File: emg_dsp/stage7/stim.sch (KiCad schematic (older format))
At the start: 7 parts

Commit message: woooo working on the next microstimulator.
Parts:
- removed U?: JUMP, 2x100mil, symbol JUMP
- added D2: D, SOD-323, symbol D
- added R5: 1k, 0402, symbol R
- added TP1: TP, TP, symbol TP
- gave numbers to parts that had none: 6
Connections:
- net Iout: now also R5.1; no longer U12.3 (FB)
- net at C19.1, D1.3 (c): now also U13.3 (d), D2.3 (c), TP1.1
- new net: D2.1 (a), R5.2, U12.3 (FB)
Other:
- note added: "30V Zener"
- note added: "eg BZT52C30S"
- moved on the sheet: C47, U41

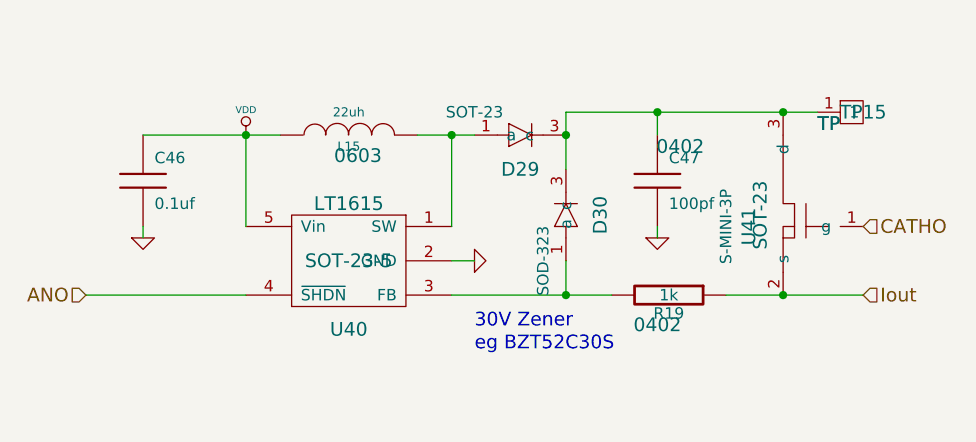
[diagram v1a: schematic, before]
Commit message: wireless stimulator!
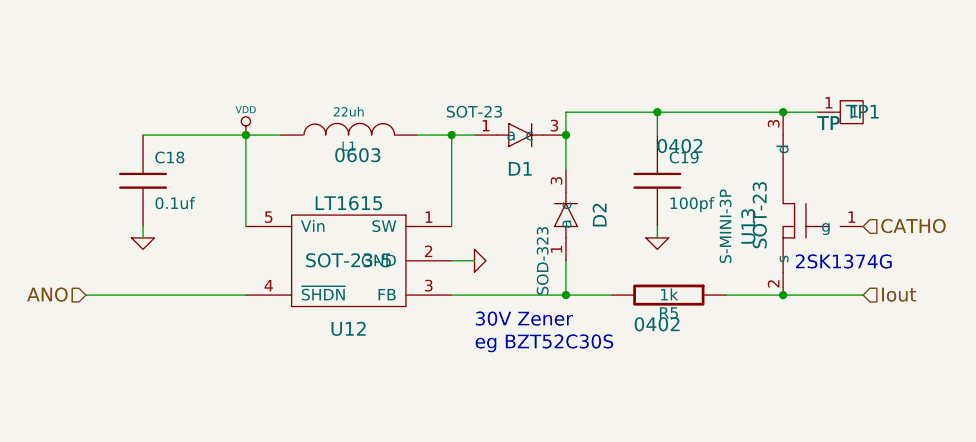
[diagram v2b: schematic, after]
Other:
- note added: "2SK1374G"
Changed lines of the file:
@@
-EESchema Schematic File Version 2  date Tue 14 Dec 2010 04:38:47 PM EST
+EESchema Schematic File Version 2  date Tue 14 Dec 2010 05:53:46 PM EST
 LIBS:power
 LIBS:device
@@
 EELAYER END
 $Descr A4 11700 8267
-Sheet 9 16
+Sheet 16 16
 Title ""
 Date "14 dec 2010"
@@
 Comment4 ""
 $EndDescr
+Text Notes 7300 3200 0    60   ~ 0
+2SK1374G
 Text Notes 5900 3550 0    60   ~ 0
 eg BZT52C30S
@@
 AR Path="/4CFFF121/4D07D318" Ref="R7"  Part="1"
 AR Path="/4CFFF11C/4D07D318" Ref="R6"  Part="1"
-F 0 "R19" V 6830 3300 50  0000 C CNN
+F 0 "R5" V 6830 3300 50  0000 C CNN
 F 1 "1k" V 6750 3300 50  0000 C CNN
 F 2 "0402" V 6880 3250 60  0000 C CNN
@@
 AR Path="/4CFFF121/4D07D2DB" Ref="D6"  Part="1"
 AR Path="/4CFFF11C/4D07D2DB" Ref="D4"  Part="1"
-F 0 "D30" H 6300 3100 60  0000 C CNN
+F 0 "D2" H 6300 3100 60  0000 C CNN
 F 1 "D" H 6300 2800 60  0001 C CNN
 F 2 "SOD-323" H 6500 2850 50  0000 C CNN
@@
 AR Path="/4CFFF121/4D07C82A" Ref="TP3"  Part="1"
 AR Path="/4CFFF11C/4D07C82A" Ref="TP2"  Part="1"
-F 0 "TP15" H 7600 2500 60  0000 C CNN
+F 0 "TP1" H 7600 2500 60  0000 C CNN
 F 1 "TP" H 7450 2450 60  0000 C CNN
 F 2 "TP" H 7450 2450 60  0000 C CNN
@@
 AR Path="/4CFFF124/4CFFEDFB" Ref="U19"  Part="1"
 AR Path="/4CFFF121/4CFFEDFB" Ref="U17"  Part="1"
-F 0 "U41" H 7000 3100 60  0000 C CNN
+F 0 "U13" H 7000 3100 60  0000 C CNN
 F 1 "SOT-23" H 7050 3150 60  0000 C CNN
 F 2 "S-MINI-3P" H 7000 3000 50  0000 C CNN
@@
 AR Path="/4CFFF124/4CFFEA48" Ref="C24"  Part="1"
 AR Path="/4CFFF121/4CFFEA48" Ref="C22"  Part="1"
-F 0 "C46" H 4500 2900 50  0000 L CNN
+F 0 "C18" H 4500 2900 50  0000 L CNN
 F 1 "0.1uf" H 4500 2700 50  0000 L CNN
 F 2 "0402" H 4550 2950 60  0001 C CNN
@@
 AR Path="/4CFFF124/4CFFEA24" Ref="C25"  Part="1"
 AR Path="/4CFFF121/4CFFEA24" Ref="C23"  Part="1"
-F 0 "C47" H 6750 2900 50  0000 L CNN
+F 0 "C19" H 6750 2900 50  0000 L CNN
 F 1 "100pf" H 6750 2700 50  0000 L CNN
 F 2 "0402" H 6800 2950 60  0000 C CNN
@@
 AR Path="/4CFFF124/4CFFE9AE" Ref="D7"  Part="1"
 AR Path="/4CFFF121/4CFFE9AE" Ref="D5"  Part="1"
-F 0 "D29" H 6100 2750 60  0000 C CNN
+F 0 "D1" H 6100 2750 60  0000 C CNN
 F 1 "BAT54" H 6100 2450 60  0001 C CNN
 F 2 "SOT-23" H 6300 2500 50  0000 C CNN
@@
 AR Path="/4CFFF124/4CFFE99A" Ref="L4"  Part="1"
 AR Path="/4CFFF121/4CFFE99A" Ref="L3"  Part="1"
-F 0 "L15" V 5300 2600 40  0000 C CNN
+F 0 "L1" V 5300 2600 40  0000 C CNN
 F 1 "22uh" V 5450 2600 40  0000 C CNN
 F 2 "0603" V 5260 2560 60  0000 C CNN
@@
 AR Path="/4CFFF124/4CFFE988" Ref="U18"  Part="1"
 AR Path="/4CFFF121/4CFFE988" Ref="U16"  Part="1"
-F 0 "U40" H 5350 2850 60  0000 C CNN
+F 0 "U12" H 5350 2850 60  0000 C CNN
 F 1 "LT1615" H 5350 3400 60  0000 C CNN
 F 2 "SOT-23-5" H 5350 3150 60  0000 C CNN

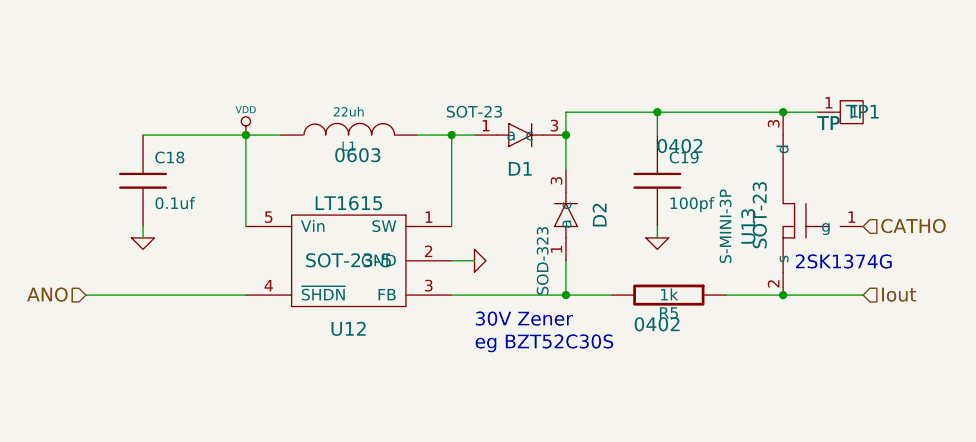
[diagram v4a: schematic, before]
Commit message: adding changes to new board -- still feel that the schematic needs to be checked over, though.
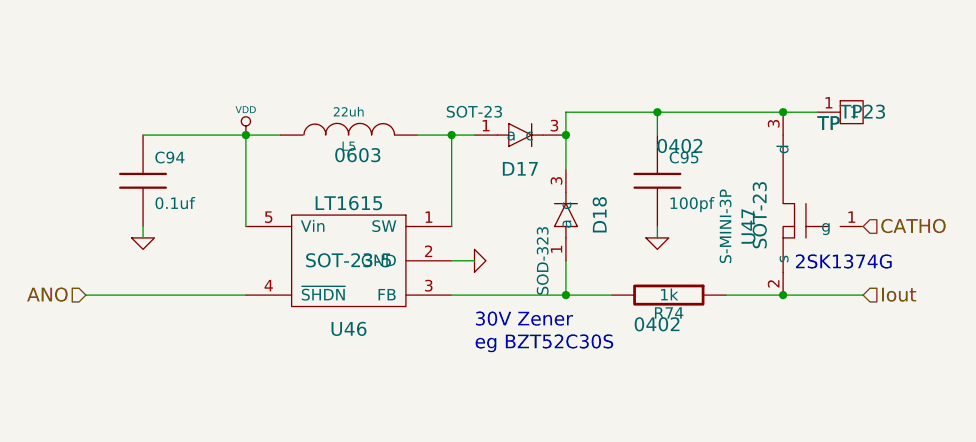
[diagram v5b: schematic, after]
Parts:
- removed C18: 0.1uf, 0402, symbol C
- removed C19: 100pf, 0402, symbol C
- removed D1: BAT54, SOT-23, symbol D
- removed D2: D, SOD-323, symbol D
- removed L1: 22uh, 0603, symbol INDUCTOR
- removed R5: 1k, 0402, symbol R
- removed TP1: TP, TP, symbol TP
- removed U13: SOT-23, S-MINI-3P, symbol 2SK3539
- added C94: 0.1uf, 0402, symbol C
- added C95: 100pf, 0402, symbol C
- added D17: BAT54, SOT-23, symbol D
- added D18: D, SOD-323, symbol D
- added L5: 22uh, 0603, symbol INDUCTOR
- added R74: 1k, 0402, symbol R
- added TP23: TP, TP, symbol TP
- added U47: SOT-23, S-MINI-3P, symbol 2SK3539
- renumbered U12 to U46
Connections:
- net CATHO: now also U47.1 (g)
- net GND: now also C94.2, C95.2
- net Iout: now also R74.1, U47.2 (s)
- net VDD: now also C94.1, L5.1
- net at U46.1 (SW): now also D17.1 (a), L5.2
- net at U46.3 (FB): now also D18.1 (a), R74.2
- new net: C95.1, D17.3 (c), D18.3 (c), TP23.1, U47.3 (d)

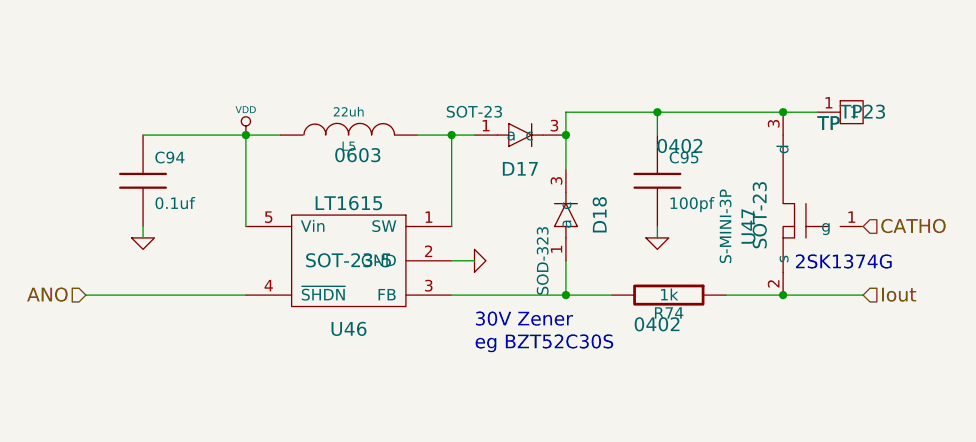
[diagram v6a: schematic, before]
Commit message: working on the stimulator - using battery isolation for now. the Burr-brown DC-DC converters tend to generate a bit of noise.
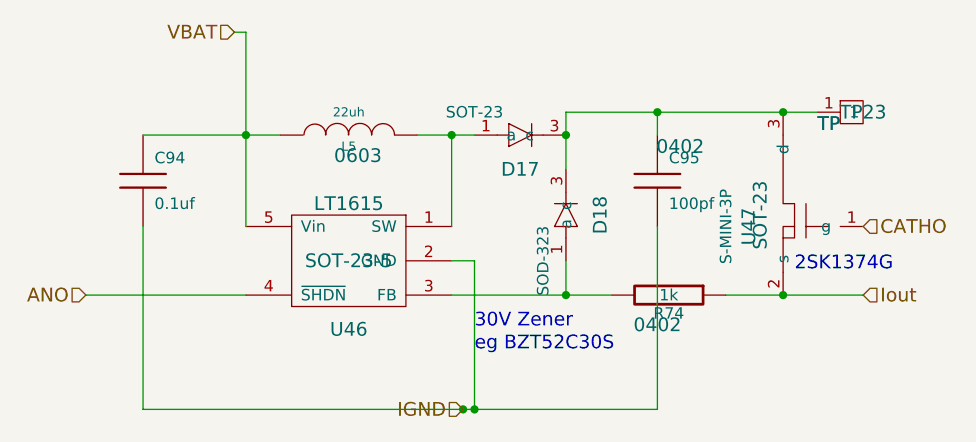
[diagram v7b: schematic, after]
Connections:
- net GND renamed IGND
- net VDD renamed VBAT
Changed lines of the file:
@@
-EESchema Schematic File Version 2  date Fri 21 Jan 2011 02:51:55 PM EST
+EESchema Schematic File Version 2  date Fri 21 Jan 2011 05:22:11 PM EST
 LIBS:power
 LIBS:device
@@
 EELAYER END
 $Descr A4 11700 8267
-Sheet 11 19
+Sheet 13 19
 Title ""
-Date "20 jan 2011"
+Date "21 jan 2011"
 Rev ""
 Comp ""
@@
 Comment4 ""
 $EndDescr
+Connection ~ 5850 3800
+Wire Wire Line
+	4450 3800 6700 3800
+Wire Wire Line
+	4450 3800 4450 3000
+Wire Wire Line
+	4900 3000 4900 2150
+Wire Wire Line
+	4900 2150 4850 2150
+Wire Wire Line
+	7600 3300 7000 3300
+Wire Wire Line
+	5800 3300 6500 3300
+Connection ~ 6300 2600
+Wire Wire Line
+	6300 2750 6300 2500
+Wire Wire Line
+	4900 3300 4200 3300
+Connection ~ 4900 2600
+Wire Wire Line
+	4450 2600 5050 2600
+Wire Wire Line
+	5800 3150 5900 3150
+Wire Wire Line
+	5650 2600 5900 2600
+Wire Wire Line
+	5800 3000 5800 2600
+Connection ~ 5800 2600
+Connection ~ 7250 3300
+Connection ~ 7250 2500
+Wire Wire Line
+	6300 2500 7400 2500
+Wire Wire Line
+	6300 3300 6300 3150
+Connection ~ 6300 3300
+Wire Wire Line
+	6700 2600 6700 2500
+Connection ~ 6700 2500
+Wire Wire Line
+	5900 3150 5900 3800
+Wire Wire Line
+	6700 3800 6700 3000
+Connection ~ 5900 3800
+Text HLabel 5850 3800 0    60   Input ~ 0
+IGND
+Text HLabel 4850 2150 0    60   Input ~ 0
+VBAT
 Text Notes 7300 3200 0    60   ~ 0
 2SK1374G
@@
 Text Notes 5900 3450 0    60   ~ 0
 30V Zener
-Wire Wire Line
-	7600 3300 7000 3300
-Wire Wire Line
-	5800 3300 6500 3300
-Wire Wire Line
-	6700 3000 6700 3050
-Connection ~ 6300 2600
-Wire Wire Line
-	6300 2750 6300 2500
-Wire Wire Line
-	4900 3300 4200 3300
-Connection ~ 4900 2600
-Wire Wire Line
-	4450 2600 5050 2600
-Wire Wire Line
-	5800 3150 5900 3150
-Wire Wire Line
-	5650 2600 5900 2600
-Wire Wire Line
-	5800 3000 5800 2600
-Connection ~ 5800 2600
-Wire Wire Line
-	4900 2600 4900 3000
-Wire Wire Line
-	4450 3000 4450 3050
-Connection ~ 7250 3300
-Connection ~ 7250 2500
-Wire Wire Line
-	6300 2500 7400 2500
-Wire Wire Line
-	6300 3300 6300 3150
-Connection ~ 6300 3300
-Wire Wire Line
-	6700 2600 6700 2500
-Connection ~ 6700 2500
 $Comp
 L R R74
@@
 AR Path="/4D2F608C/4CFFFADB/4D361954" Ref="R74"  Part="1"
 AR Path="/4D2F608C/4CFFE972/4D361954" Ref="R74"  Part="1"
+AR Path="/4D2F608C/4D07DB98/4D361954" Ref="R74"  Part="1"
+AR Path="/4D2F608C/4CFFF11C/4D361954" Ref="R74"  Part="1"
+AR Path="/4D2F608C/4CFFFADE/4D361954" Ref="R74"  Part="1"
 F 0 "R74" V 6830 3300 50  0000 C CNN
 F 1 "1k" V 6750 3300 50  0000 C CNN
@@
 AR Path="/4D2F608C/4CFFFADB/4D36194B" Ref="D18"  Part="1"
 AR Path="/4D2F608C/4CFFE972/4D36194B" Ref="D18"  Part="1"
+AR Path="/4D2F608C/4D07DB98/4D36194B" Ref="D18"  Part="1"
+AR Path="/4D2F608C/4CFFF11C/4D36194B" Ref="D18"  Part="1"
+AR Path="/4D2F608C/4CFFFADE/4D36194B" Ref="D18"  Part="1"
 F 0 "D18" H 6300 3100 60  0000 C CNN
 F 1 "D" H 6300 2800 60  0001 C CNN
@@
 AR Path="/4D2F608C/4CFFFADB/4D361938" Ref="TP23"  Part="1"
 AR Path="/4D2F608C/4CFFE972/4D361938" Ref="TP23"  Part="1"
+AR Path="/4D2F608C/4D07DB98/4D361938" Ref="TP23"  Part="1"
+AR Path="/4D2F608C/4CFFF11C/4D361938" Ref="TP23"  Part="1"
+AR Path="/4D2F608C/4CFFFADE/4D361938" Ref="TP23"  Part="1"
 F 0 "TP23" H 7600 2500 60  0000 C CNN
 F 1 "TP" H 7450 2450 60  0000 C CNN
@@
 $EndComp
 $Comp
-L VDD #PWR0218
-U 1 1 4D361928
-P 4900 2600
-AR Path="/4D2F608C/4CFFFADB/4D361928" Ref="#PWR0218"  Part="1"
-AR Path="/4D2F608C/4CFFE972/4D361928" Ref="#PWR0218"  Part="1"
-F 0 "#PWR0218" H 4900 2700 30  0001 C CNN
-F 1 "VDD" H 4900 2710 30  0000 C CNN
-	1    4900 2600
-	1    0    0    -1
-$EndComp
-$Comp
 L 2SK3539 U47
 U 1 1 4D361921
@@
 AR Path="/4D2F608C/4CFFFADB/4D361921" Ref="U47"  Part="1"
 AR Path="/4D2F608C/4CFFE972/4D361921" Ref="U47"  Part="1"
+AR Path="/4D2F608C/4D07DB98/4D361921" Ref="U47"  Part="1"
+AR Path="/4D2F608C/4CFFF11C/4D361921" Ref="U47"  Part="1"
+AR Path="/4D2F608C/4CFFFADE/4D361921" Ref="U47"  Part="1"
 F 0 "U47" H 7000 3100 60  0000 C CNN
 F 1 "SOT-23" H 7050 3150 60  0000 C CNN
@@
 $EndComp
 $Comp
-L GND #PWR0219
-U 1 1 4D361919
-P 4450 3050
-AR Path="/4D2F608C/4CFFFADB/4D361919" Ref="#PWR0219"  Part="1"
-AR Path="/4D2F608C/4CFFE972/4D361919" Ref="#PWR0219"  Part="1"
-F 0 "#PWR0219" H 4450 3050 30  0001 C CNN
-F 1 "GND" H 4450 2980 30  0001 C CNN
-	1    4450 3050
-	1    0    0    -1
-$EndComp
-$Comp
 L C C94
 U 1 1 4D36190A
@@
 AR Path="/4D2F608C/4CFFFADB/4D36190A" Ref="C94"  Part="1"
 AR Path="/4D2F608C/4CFFE972/4D36190A" Ref="C94"  Part="1"
+AR Path="/4D2F608C/4D07DB98/4D36190A" Ref="C94"  Part="1"
+AR Path="/4D2F608C/4CFFF11C/4D36190A" Ref="C94"  Part="1"
+AR Path="/4D2F608C/4CFFFADE/4D36190A" Ref="C94"  Part="1"
 F 0 "C94" H 4500 2900 50  0000 L CNN
 F 1 "0.1uf" H 4500 2700 50  0000 L CNN
@@
 $EndComp
 $Comp
-L GND #PWR0220
-U 1 1 4D3618FA
-P 6700 3050
-AR Path="/4D2F608C/4CFFFADB/4D3618FA" Ref="#PWR0220"  Part="1"
-AR Path="/4D2F608C/4CFFE972/4D3618FA" Ref="#PWR0220"  Part="1"
-F 0 "#PWR0220" H 6700 3050 30  0001 C CNN
-F 1 "GND" H 6700 2980 30  0001 C CNN
-	1    6700 3050
-	1    0    0    -1
-$EndComp
-$Comp
 L C C95
 U 1 1 4D3618E7
@@
 AR Path="/4D2F608C/4CFFFADB/4D3618E7" Ref="C95"  Part="1"
 AR Path="/4D2F608C/4CFFE972/4D3618E7" Ref="C95"  Part="1"
+AR Path="/4D2F608C/4D07DB98/4D3618E7" Ref="C95"  Part="1"
+AR Path="/4D2F608C/4CFFF11C/4D3618E7" Ref="C95"  Part="1"
+AR Path="/4D2F608C/4CFFFADE/4D3618E7" Ref="C95"  Part="1"
 F 0 "C95" H 6750 2900 50  0000 L CNN
 F 1 "100pf" H 6750 2700 50  0000 L CNN
@@
 ANO
 $Comp
-L GND #PWR0221
-U 1 1 4D3618D6
-P 5900 3150
-AR Path="/4D2F608C/4CFFFADB/4D3618D6" Ref="#PWR0221"  Part="1"
-AR Path="/4D2F608C/4CFFE972/4D3618D6" Ref="#PWR0221"  Part="1"
-F 0 "#PWR0221" H 5900 3150 30  0001 C CNN
-F 1 "GND" H 5900 3080 30  0001 C CNN
-	1    5900 3150
-	0    -1   -1   0
-$EndComp
-$Comp
 L D D17
 U 1 1 4D3618C7
@@
 AR Path="/4D2F608C/4CFFFADB/4D3618C7" Ref="D17"  Part="1"
 AR Path="/4D2F608C/4CFFE972/4D3618C7" Ref="D17"  Part="1"
+AR Path="/4D2F608C/4D07DB98/4D3618C7" Ref="D17"  Part="1"
+AR Path="/4D2F608C/4CFFF11C/4D3618C7" Ref="D17"  Part="1"
+AR Path="/4D2F608C/4CFFFADE/4D3618C7" Ref="D17"  Part="1"
 F 0 "D17" H 6100 2750 60  0000 C CNN
 F 1 "BAT54" H 6100 2450 60  0001 C CNN
@@
 AR Path="/4D2F608C/4CFFFADB/4D3618C2" Ref="L5"  Part="1"
 AR Path="/4D2F608C/4CFFE972/4D3618C2" Ref="L5"  Part="1"
+AR Path="/4D2F608C/4D07DB98/4D3618C2" Ref="L5"  Part="1"
+AR Path="/4D2F608C/4CFFF11C/4D3618C2" Ref="L5"  Part="1"
+AR Path="/4D2F608C/4CFFFADE/4D3618C2" Ref="L5"  Part="1"
 F 0 "L5" V 5300 2600 40  0000 C CNN
 F 1 "22uh" V 5450 2600 40  0000 C CNN
@@
 AR Path="/4D2F608C/4CFFFADB/4CFFE988" Ref="U46"  Part="1"
 AR Path="/4D2F608C/4CFFE972/4CFFE988" Ref="U46"  Part="1"
+AR Path="/4D2F608C/4D07DB98/4CFFE988" Ref="U46"  Part="1"
+AR Path="/4D2F608C/4CFFF11C/4CFFE988" Ref="U46"  Part="1"
+AR Path="/4D2F608C/4CFFFADE/4CFFE988" Ref="U46"  Part="1"
 F 0 "U46" H 5350 2850 60  0000 C CNN
 F 1 "LT1615" H 5350 3400 60  0000 C CNN

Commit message: starting placement of modules in board...
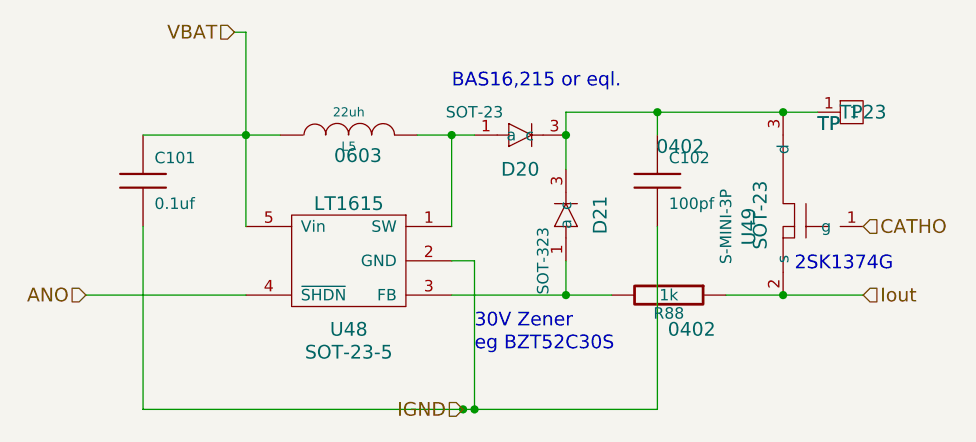
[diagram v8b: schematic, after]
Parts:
- D49: renamed from D18; footprint SOD-323 -> SOT-323
- renumbered C94 to C129, C95 to C130, D17 to D48, L5 to L19, R74 to R102, TP23 to TP37, U46 to U76, U47 to U77
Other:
- note added: "BAS16,215 or eql."
